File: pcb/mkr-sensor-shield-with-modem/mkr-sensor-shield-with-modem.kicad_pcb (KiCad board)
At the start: 2 copper layers, 100 x 80 mm, 32 parts, among them J1 Conn_01x03_Pin, J10 Conn_01x03_Pin, J11 Conn_01x03_Pin, J12 Conn_01x03_Pin, J13 Conn_01x03_Pin, J14 Conn_01x03_Pin, J15 Conn_01x03_Pin, J16 Conn_01x03_Pin, J17 Conn_01x03_Pin, J18 Conn_01x03_Pin, J19 Conn_02x06_Odd_Even, J2 Conn_01x03_Pin, J20 Conn_02x03_Odd_Even, J21 Conn_01x02_Pin, J23 Conn_01x02_Pin, J3 Conn_01x03_Pin, J4 Conn_01x03_Pin, J5 Conn_01x03_Pin, J6 Conn_01x03_Pin, J7 Conn_01x03_Pin, J8 Conn_01x03_Pin, J9 Conn_01x03_Pin, SW1 SW_Push, U1 L7805

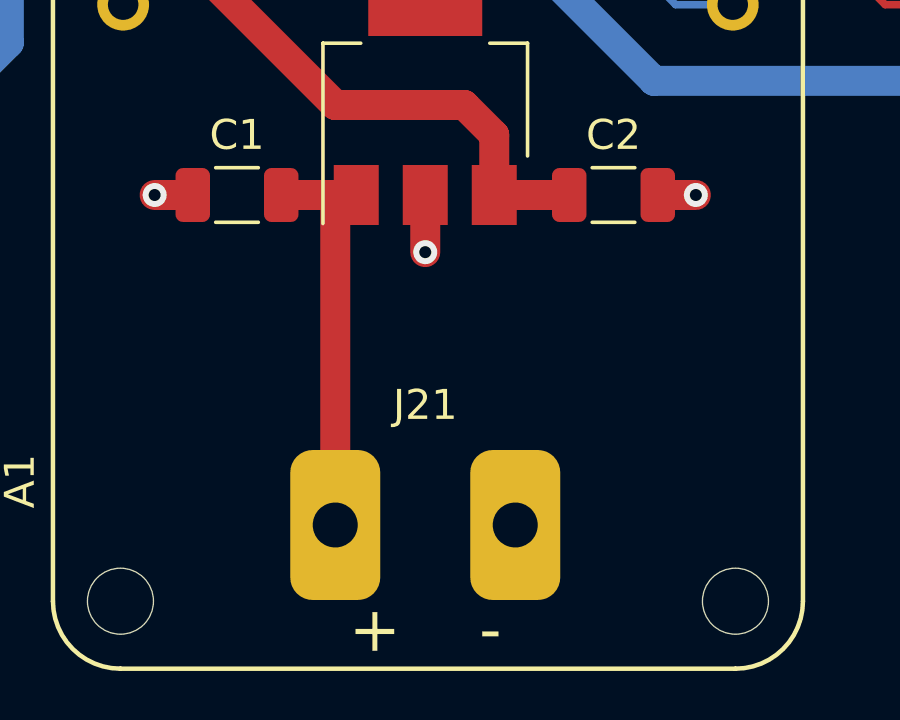
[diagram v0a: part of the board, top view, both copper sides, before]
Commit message: Remove backups from repo.  Add jumper to bypass voltage regulator
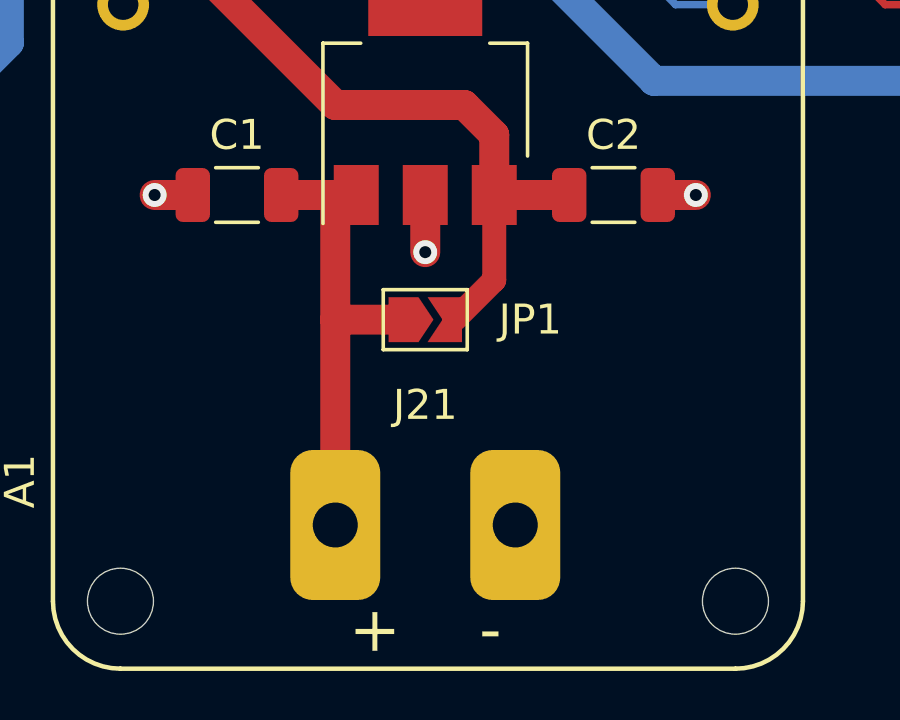
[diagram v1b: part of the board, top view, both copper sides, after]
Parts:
- added JP1: SolderJumper_2_Open, Jumper:SolderJumper-2_P1.3mm_Open_TrianglePad1.0x1.5mm, F.Cu at (150.9, 107.8)
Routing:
- net Net-(JP1-B): track 19.7 -> 24.4 mm
- net Net-(J21-Pin_1): track 13.5 -> 15.8 mm
